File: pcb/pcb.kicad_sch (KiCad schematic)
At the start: 16 parts, among them J1 encoder, J2 programmer, J3 oled display, J4 usb-ttl, SW1 reset, SW2 play/pause, SW3 prev track, SW4 next track, U1 ATmega32-16P

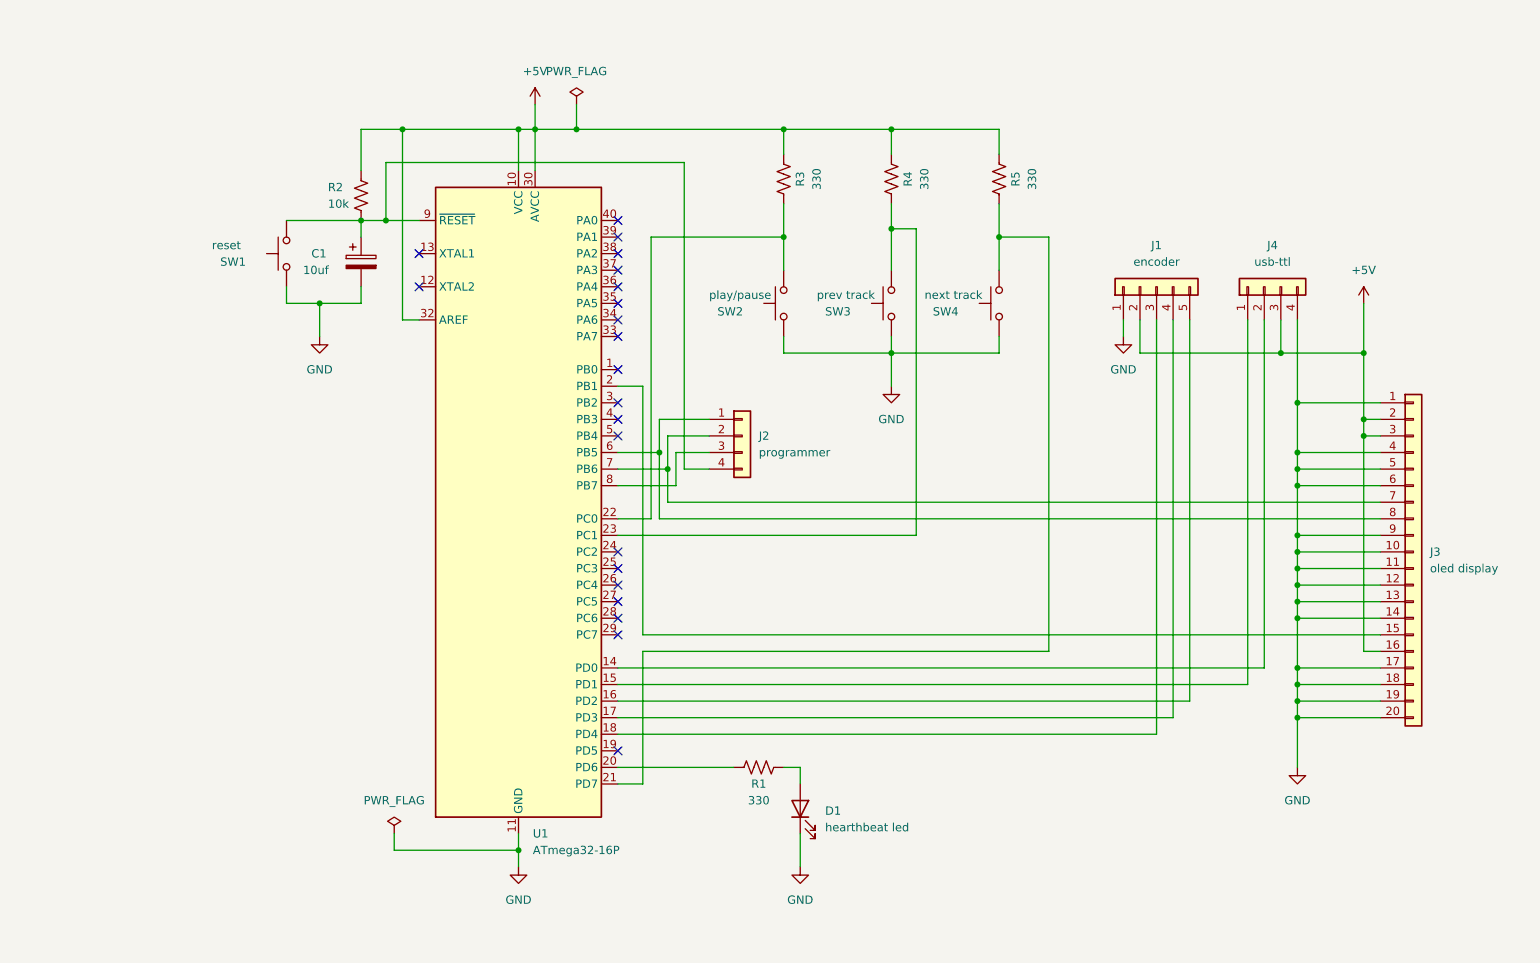
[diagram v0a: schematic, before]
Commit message: add oled footprint
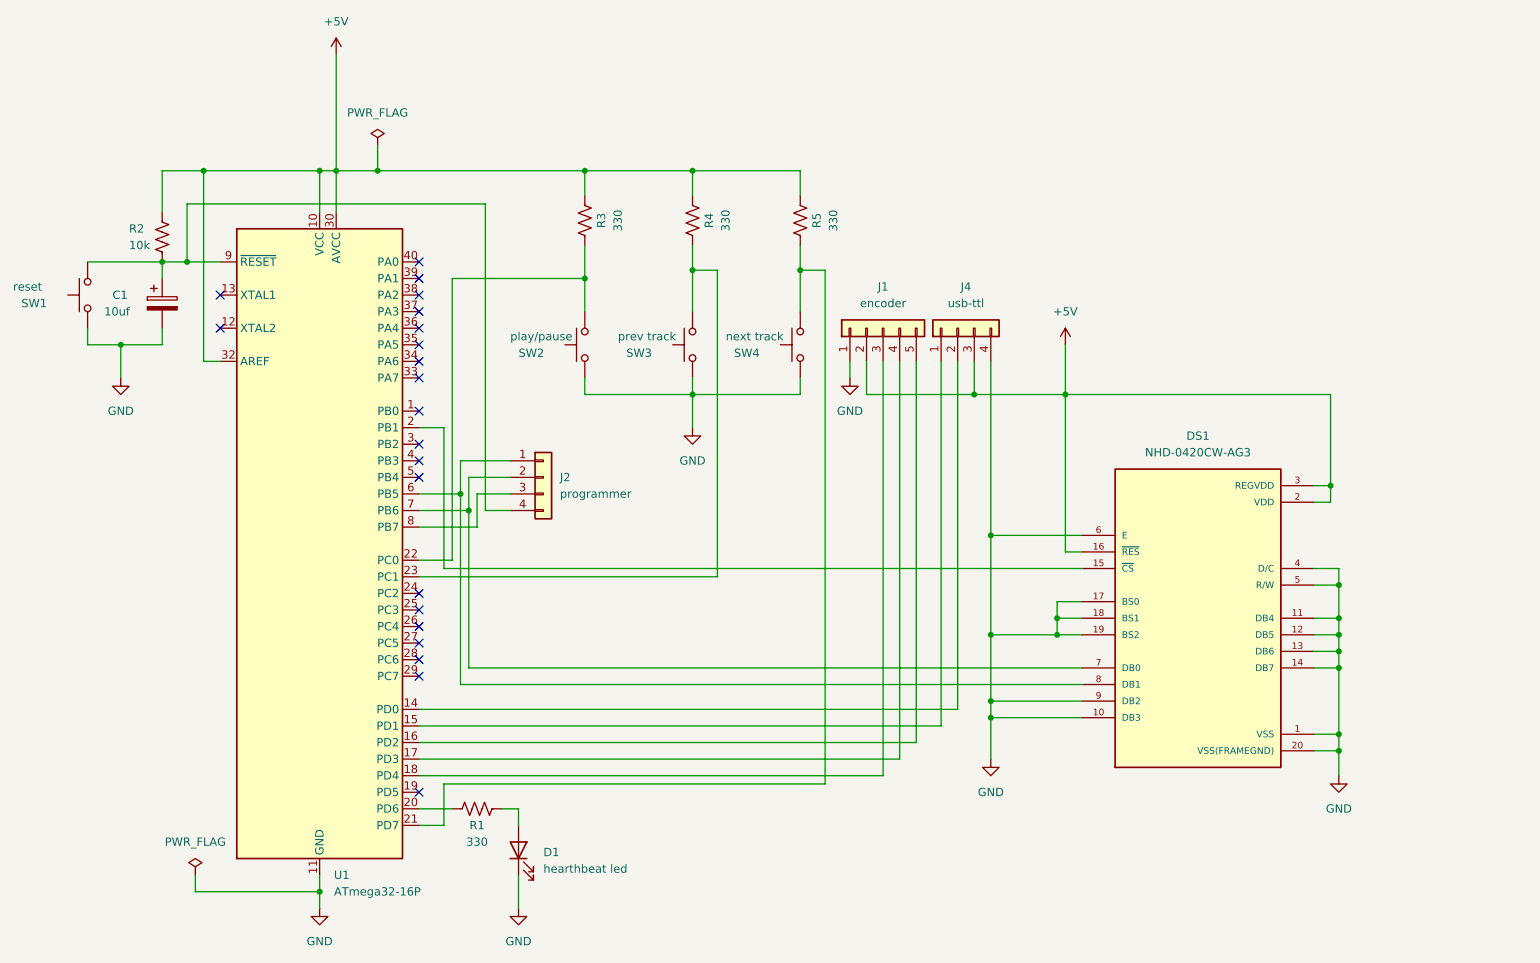
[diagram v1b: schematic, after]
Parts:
- removed J3: oled display, Connector_PinHeader_2.54mm:PinHeader_1x20_P2.54mm_Vertical, symbol Connector_Generic:Conn_01x20
- added DS1: NHD-0420CW-AG3, Library:NHD-0420CW-AG3, symbol NHD-0420CW-AG3:NHD-0420CW-AG3
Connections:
- net +5V: now also DS1.16 (~{RES}), DS1.2 (VDD), DS1.3 (REGVDD)
- net GND: now also DS1.1 (VSS), DS1.10 (DB3), DS1.11 (DB4), DS1.12 (DB5), DS1.13 (DB6), DS1.14 (DB7), DS1.17 (BS0), DS1.18 (BS1), DS1.19 (BS2), DS1.20 (VSS(FRAMEGND)), DS1.4 (D/C), DS1.5 (R/W), DS1.6 (E), DS1.9 (DB2)
- net at U1.2 (PB1): now also DS1.15 (~{CS})
- net at J2.2 (Pin_2), U1.7 (PB6): now also DS1.7 (DB0)
- net at J2.1 (Pin_1), U1.6 (PB5): now also DS1.8 (DB1)
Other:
- moved on the sheet: C1, D1, J1, J2, J4, R1, R2, R3, R4, R5, SW1, SW2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

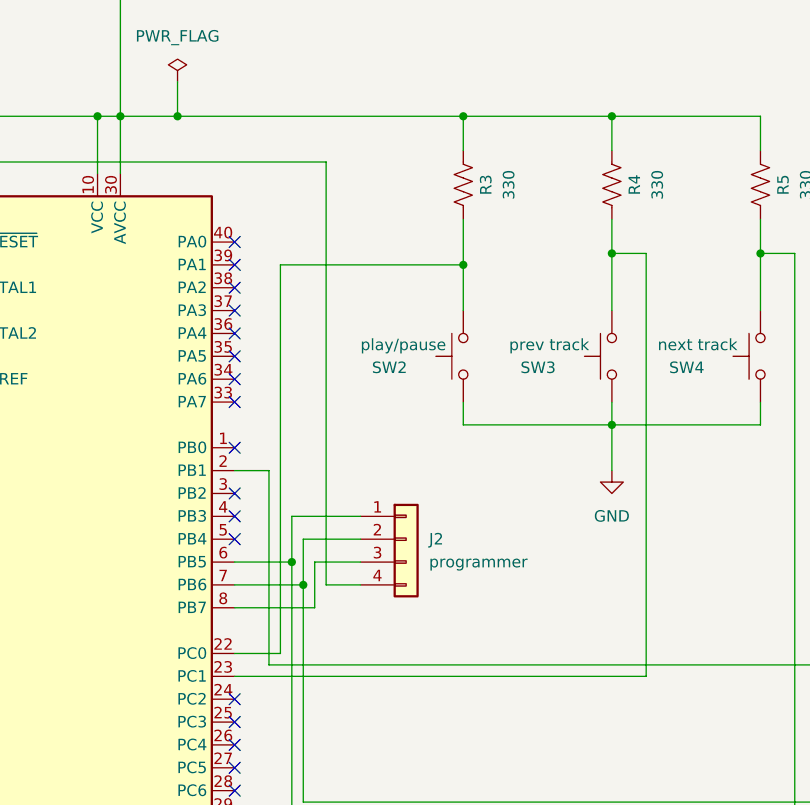
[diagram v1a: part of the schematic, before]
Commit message: actualizacion de archivos con footprint OLED
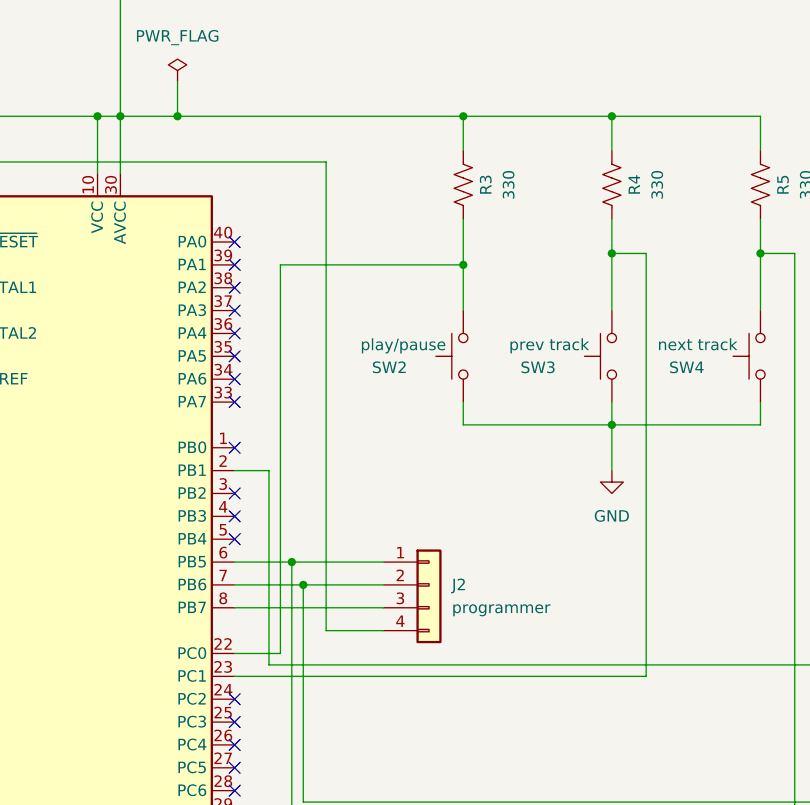
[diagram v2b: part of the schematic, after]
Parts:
- DS1: footprint Library:NHD-0420CW-AG3 -> NHD_NHD-0420CW-AG3
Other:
- moved on the sheet: J2
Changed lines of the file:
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@@
     (stroke (width 0) (type default))
   )
-  (wire (pts (xy 110.49 54.61) (xy 110.49 101.6))
+  (wire (pts (xy 110.49 54.61) (xy 110.49 106.68))
     (stroke (width 0) (type default))
   )
@@
     (stroke (width 0) (type default))
   )
-  (wire (pts (xy 114.3 101.6) (xy 110.49 101.6))
+  (wire (pts (xy 116.84 106.68) (xy 110.49 106.68))
     (stroke (width 0) (type default))
   )
@@
     (stroke (width 0) (type default))
   )
-  (wire (pts (xy 106.68 93.98) (xy 106.68 99.06))
-    (stroke (width 0) (type default))
-  )
   (wire (pts (xy 60.96 73.66) (xy 60.96 76.2))
     (stroke (width 0) (type default))
@@
     (stroke (width 0) (type default))
   )
-  (wire (pts (xy 109.22 104.14) (xy 109.22 99.06))
-    (stroke (width 0) (type default))
-  )
   (wire (pts (xy 60.96 63.5) (xy 64.77 63.5))
     (stroke (width 0) (type default))
@@
     (stroke (width 0) (type default))
   )
-  (wire (pts (xy 109.22 99.06) (xy 114.3 99.06))
-    (stroke (width 0) (type default))
-  )
   (wire (pts (xy 105.41 109.22) (xy 105.41 66.04))
     (stroke (width 0) (type default))
@@
     (stroke (width 0) (type default))
   )
-  (wire (pts (xy 100.33 104.14) (xy 109.22 104.14))
+  (wire (pts (xy 100.33 104.14) (xy 116.84 104.14))
     (stroke (width 0) (type default))
   )
@@
     (stroke (width 0) (type default))
   )
-  (wire (pts (xy 114.3 93.98) (xy 106.68 93.98))
+  (wire (pts (xy 116.84 99.06) (xy 106.68 99.06))
     (stroke (width 0) (type default))
   )
@@
     (stroke (width 0) (type default))
   )
-  (wire (pts (xy 107.95 96.52) (xy 114.3 96.52))
+  (wire (pts (xy 107.95 101.6) (xy 116.84 101.6))
     (stroke (width 0) (type default))
   )
@@
   )
   (wire (pts (xy 237.49 118.11) (xy 241.3 118.11))
-    (stroke (width 0) (type default))
-  )
-  (wire (pts (xy 107.95 101.6) (xy 107.95 96.52))
     (stroke (width 0) (type default))
   )
@@
       (effects (font (size 1.27 1.27)))
     )
-    (property "Footprint" "Library:NHD-0420CW-AG3" (at 219.71 118.11 0)
+    (property "Footprint" "NHD_NHD-0420CW-AG3" (at 219.71 118.11 0)
       (effects (font (size 1.27 1.27)) (justify left bottom) hide)
     )
@@
     )
   )
-  (symbol (lib_id "Connector_Generic:Conn_01x04") (at 119.38 96.52 0) (unit 1)
-    (in_bom yes) (on_board yes) (dnp no) (fields_autoplaced)
-    (property "Reference" "J2" (at 121.92 96.52 0)
+  (symbol (lib_id "Connector_Generic:Conn_01x04") (at 121.92 101.6 0) (unit 1)
+    (in_bom yes) (on_board yes) (dnp no) (fields_autoplaced)
+    (property "Reference" "J2" (at 124.46 101.6 0)
       (effects (font (size 1.27 1.27)) (justify left))
     )
-    (property "Value" "programmer" (at 121.92 99.06 0)
+    (property "Value" "programmer" (at 124.46 104.14 0)
       (effects (font (size 1.27 1.27)) (justify left))
     )
-    (property "Footprint" "Connector_PinHeader_2.54mm:PinHeader_1x04_P2.54mm_Vertical" (at 119.38 96.52 0)
-      (effects (font (size 1.27 1.27)) hide)
-    )
-    (property "Datasheet" "~" (at 119.38 96.52 0)
-      (effects (font (size 1.27 1.27)) hide)
-    )
+    (property "Footprint" "Connector_PinHeader_2.54mm:PinHeader_1x04_P2.54mm_Vertical" (at 121.92 101.6 0)
+      (effects (font (size 1.27 1.27)) hide)
+    )
+    (property "Datasheet" "~" (at 121.92 101.6 0)
+      (effects (font (size 1.27 1.27)) hide)
+    )

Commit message: agrego timer de apagado si no hay conexion a pc
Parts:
- DS1: footprint NHD_NHD-0420CW-AG3 -> Library:NHD-0420CW-AG3
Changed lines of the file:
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@@
       (effects (font (size 1.27 1.27)))
     )
-    (property "Footprint" "NHD_NHD-0420CW-AG3" (at 219.71 118.11 0)
+    (property "Footprint" "Library:NHD-0420CW-AG3" (at 219.71 118.11 0)
       (effects (font (size 1.27 1.27)) (justify left bottom) hide)
     )

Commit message: retomando proyecto
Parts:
- DS1: footprint Library:NHD-0420CW-AG3 -> NHD_NHD-0420CW-AG3; PARTREV 3 -> (none)
- J1: footprint Connector_PinSocket_2.54mm:PinSocket_1x05_P2.54mm_Vertical -> (none)

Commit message: final
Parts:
- D1: value hearthbeat led -> heartbeat led
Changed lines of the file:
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@@
 		(fields_autoplaced yes)
 		(property "Reference" "D1"
-			(at 119.38 153.9875 90)
+			(at 119.38 153.9874 90)
 			(effects
 				(font
@@
 			)
 		)
-		(property "Value" "hearthbeat led"
-			(at 119.38 156.5275 90)
+		(property "Value" "heartbeat led"
+			(at 119.38 156.5274 90)
 			(effects
 				(font
